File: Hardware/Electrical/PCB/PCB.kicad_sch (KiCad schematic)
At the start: 2 parts

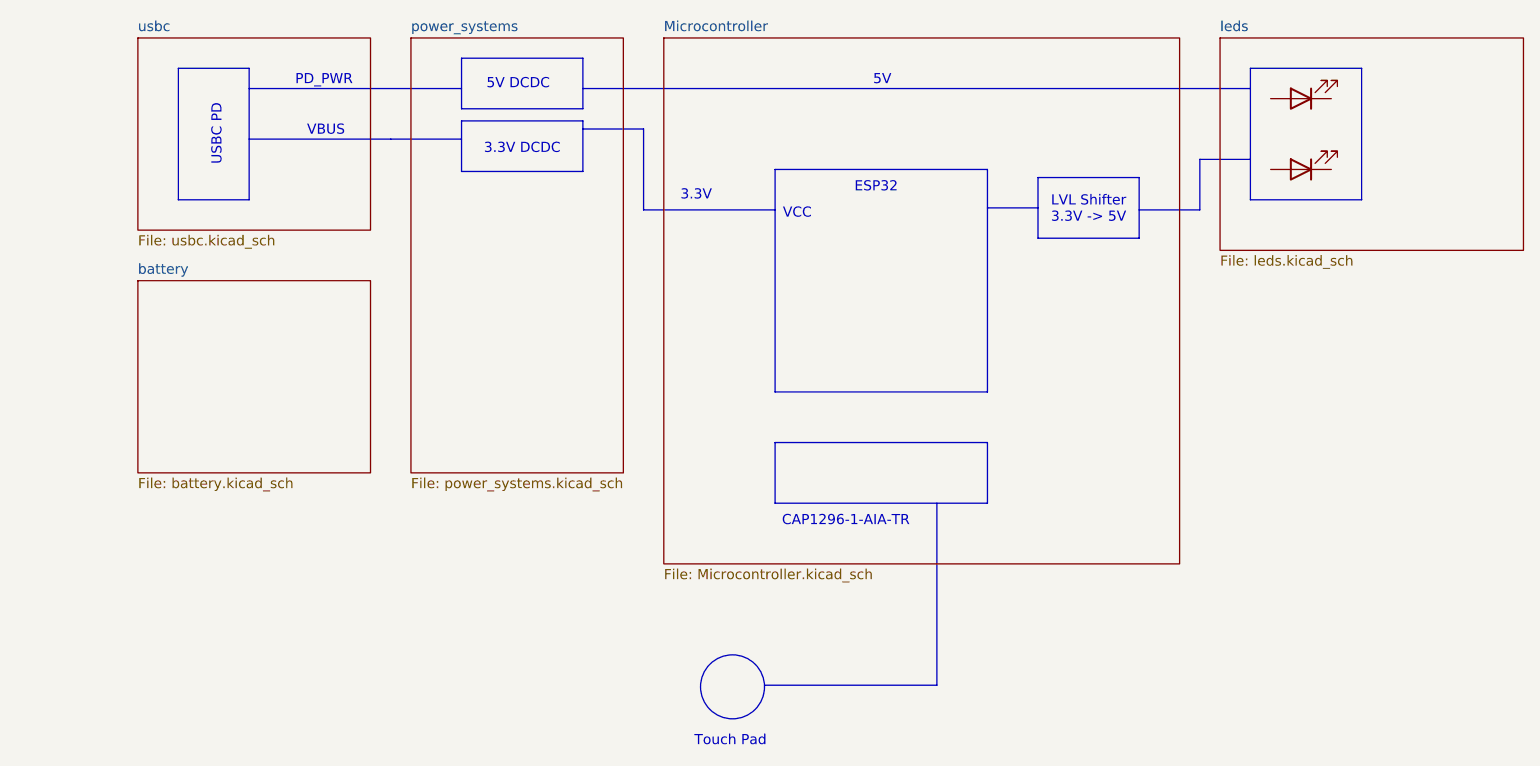
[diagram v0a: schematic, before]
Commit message: battery charger added
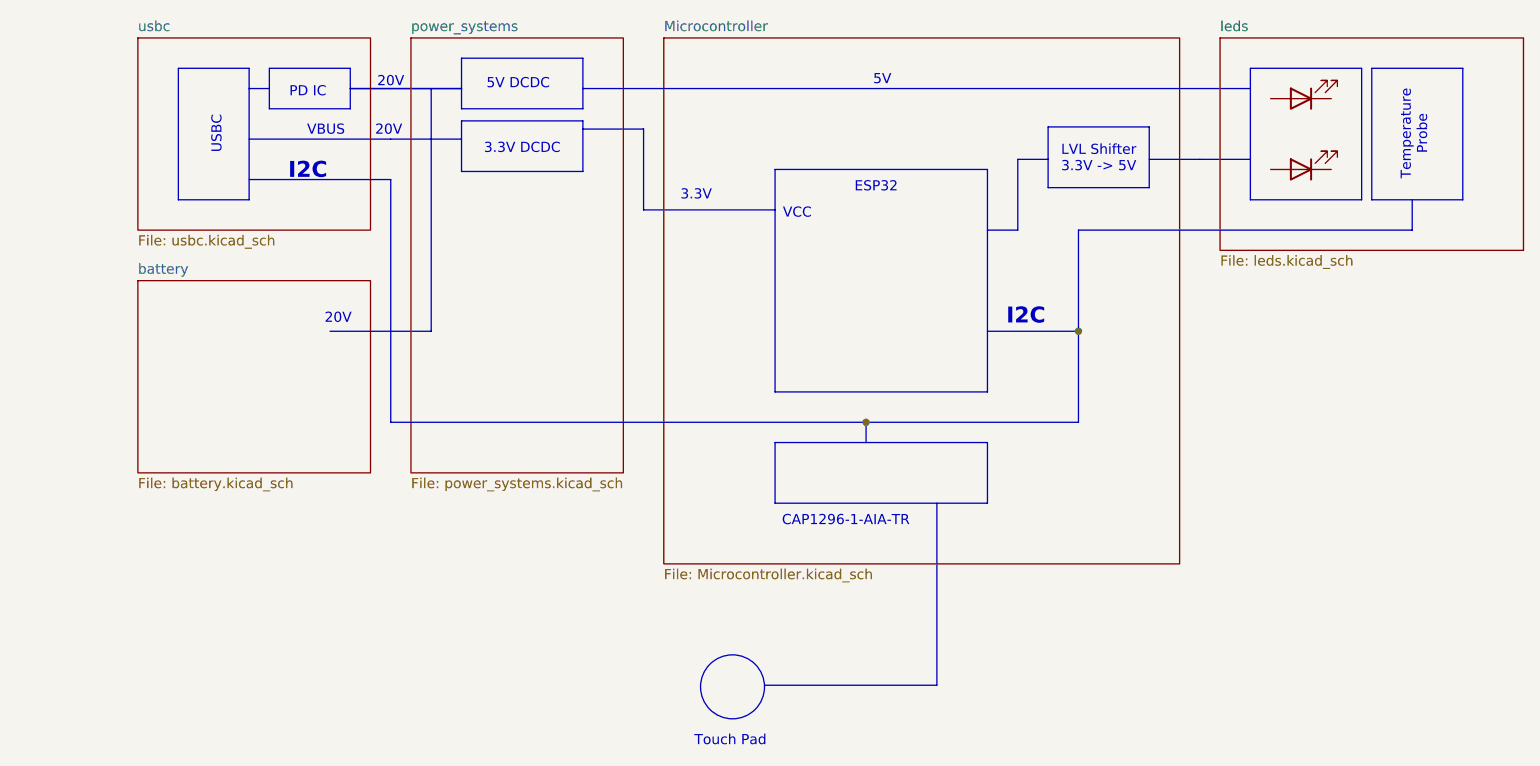
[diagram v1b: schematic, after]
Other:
- note added: "20V"
- note added: "I2C"
- note added: "PD IC"
- note added: "Temperature Probe"
- note added: "USBC"
- note removed: "PD_PWR"
- note removed: "USBC PD"

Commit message: project state at start of school project
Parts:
- added BT5: Battery_Cell, symbol Device:Battery_Cell
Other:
- note added: "Balancer"
- note added: "Charger"
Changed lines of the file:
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@@
+	)
+	(rectangle
+		(start 59.69 109.22)
+		(end 71.12 116.84)
+		(stroke
+			(width 0)
+			(type default)
+		)
+		(fill
+			(type none)
+		)
 	)
 	(rectangle
 		(start 199.39 71.12)
 		(end 210.82 87.63)
+		(stroke
+			(width 0)
+			(type default)
+		)
+		(fill
+			(type none)
+		)
+	)
+	(rectangle
+		(start 45.72 101.6)
+		(end 52.07 118.11)
 		(stroke
 			(width 0)
@@
 		)
 	)
+	(text "Balancer"
+		(exclude_from_sim no)
+		(at 65.532 113.03 0)
+		(effects
+			(font
+				(size 1.27 1.27)
+				(thickness 0.254)
+				(bold yes)
+			)
+		)
+	)
 	(text "5V DCDC"
 		(exclude_from_sim no)
@@
 		)
 	)
+	(text "Charger"
+		(exclude_from_sim no)
+		(at 48.768 110.49 90)
+		(effects
+			(font
+				(size 1.27 1.27)
+				(thickness 0.254)
+				(bold yes)
+			)
+		)
+	)
 	(text "20V"
 		(exclude_from_sim no)
@@
 		)
 	)
+	(bus
+		(pts
+			(xy 62.23 76.2) (xy 62.23 85.09)
+		)
+		(stroke
+			(width 0)
+			(type default)
+		)
+	)
+	(polyline
+		(pts
+			(xy 52.07 104.14) (xy 68.58 104.14)
+		)
+		(stroke
+			(width 0)
+			(type default)
+		)
+	)
 	(polyline
 		(pts
@@
 	(polyline
 		(pts
+			(xy 52.07 106.68) (xy 60.96 106.68)
+		)
+		(stroke
+			(width 0)
+			(type default)
+		)
+	)
+	(polyline
+		(pts
 			(xy 107.95 88.9) (xy 107.95 78.74)
 		)
@@
 	(polyline
 		(pts
+			(xy 60.96 106.68) (xy 60.96 109.22)
+		)
+		(stroke
+			(width 0)
+			(type default)
+		)
+	)
+	(polyline
+		(pts
 			(xy 76.2 80.01) (xy 85.09 80.01)
 		)
@@
 		)
 	)
-	(bus
-		(pts
-			(xy 58.42 85.09) (xy 76.2 85.09)
-		)
-		(stroke
-			(width 0)
-			(type default)
-		)
-	)
 	(polyline
 		(pts
@@
 		)
 	)
+	(bus
+		(pts
+			(xy 76.2 85.09) (xy 62.23 85.09)
+		)
+		(stroke
+			(width 0)
+			(type default)
+		)
+	)
 	(polyline
 		(pts
@@
 		)
 	)
+	(polyline
+		(pts
+			(xy 52.07 114.3) (xy 59.69 114.3)
+		)
+		(stroke
+			(width 0)
+			(type default)
+		)
+	)
 	(bus
 		(pts
@@
 		)
 	)
+	(symbol
+		(lib_id "Device:Battery_Cell")
+		(at 55.88 111.76 0)
+		(unit 1)
+		(exclude_from_sim no)
+		(in_bom yes)
+		(on_board yes)
+		(dnp no)
+		(fields_autoplaced yes)
+		(property "Reference" "BT5"
+			(at 59.69 108.6484 0)
+			(effects
+				(font
+					(size 1.27 1.27)
+				)
+				(justify left)
+				(hide yes)
+			)
+		)
+		(property "Value" "Battery_Cell"
+			(at 59.69 111.1884 0)
+			(effects
+				(font
+					(size 1.27 1.27)
+				)
+				(justify left)
+				(hide yes)
+			)
+		)
+		(property "Footprint" ""
+			(at 55.88 110.236 90)
+			(effects
+				(font
+					(size 1.27 1.27)
+				)
+				(hide yes)
+			)
+		)
+		(property "Datasheet" "~"
+			(at 55.88 110.236 90)
+			(effects
+				(font
+					(size 1.27 1.27)
+				)
+				(hide yes)
+			)
+		)
+		(property "Description" "Single-cell battery"
+			(at 55.88 111.76 0)
+			(effects
+				(font
+					(size 1.27 1.27)
+				)
+				(hide yes)
+			)
+		)
+		(pin "1"
+		)
+		(pin "2"
+		)
+		(instances
+			(project ""
+				(path "/8e3abcc5-43e9-4b34-9640-a0acd90473e7"
+					(reference "BT5")
+					(unit 1)
+				)
+			)
+		)
+	)

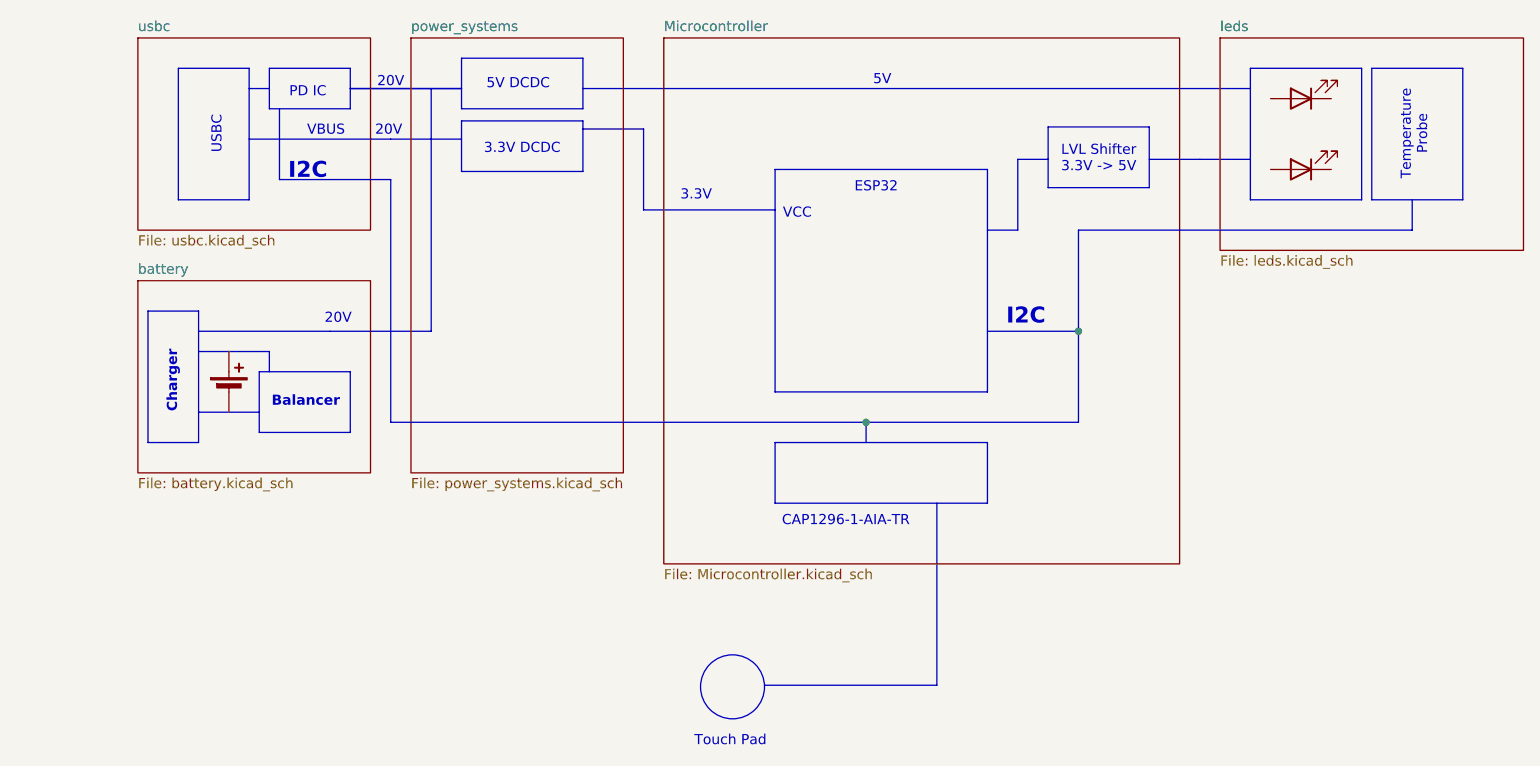
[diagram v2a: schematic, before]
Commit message: Basic Schematic finished, external connectors missing, no footprints or LCSC numbers yet
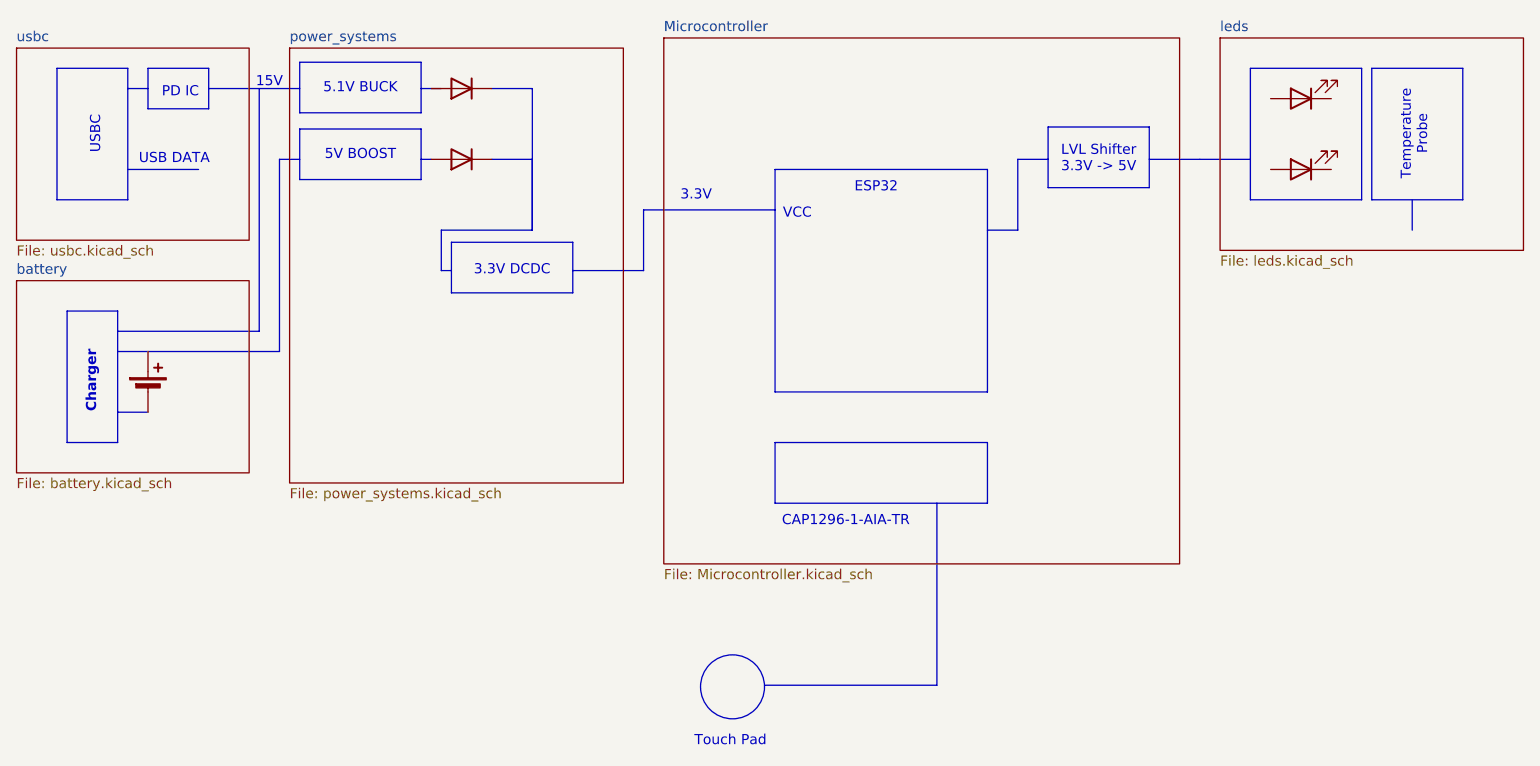
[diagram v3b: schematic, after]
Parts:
- added D4, D5: D, symbol Device:D
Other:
- note added: "15V"
- note added: "5.1V BUCK"
- note added: "5V BOOST"
- note added: "USB DATA"
- note removed: "20V"
- note removed: "5V"
- note removed: "5V DCDC"
- note removed: "Balancer"
- note removed: "I2C"
- note removed: "VBUS"

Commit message: layout v1 finished but not confirmed yet
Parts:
- BT5, D1, D2, D4, D5: now left out of the parts list
